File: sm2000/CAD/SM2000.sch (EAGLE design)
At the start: 405 parts, among them CN1 HDR100-3, CN2 ST-3509, CN3 HDR100-3, CN4 JS-MU3-002, CN5 DS-0518, CN6 ST-3509, CN7 ST-3509, J1 JMP-2PIN, J10 JMPR-2X2, J11 JMPR-2X2, J12 JMPR-2X2, J13 JMPR-2X2, J14 JMPR-2X2, J2 HDR100-7, J3 JMP-2PIN, J4 CONN-BOOM-XH-2A, J5 JMP-2PIN, J6 JMPR-2X2, J7 JMPR-2X2, J8 JMPR-2X2, J9 JMPR-2X2, P1 TPAD50, P10 TPAD50, P13 TPAD50, P2 TPAD50, P3 TPAD50, P4 TPAD50, P5 TPAD50, P6 TPAD50, P7 TPAD50, P8 TPAD50, P9 TPAD50, Q1 MMBT3904, Q10 MMBT3904, Q11 BFR92, Q12 BFQ19, Q13 RD01MUS2, Q14 MMBT3904, Q15 MMBT3904, Q16 MMBT3904, Q17 MMBT3906, Q2 STR2P3LLH6, Q3 MMBT3904, Q4 STR2P3LLH6, Q5 MMBT3904, Q6 MMBT3904, Q7 MMBT3904, Q8 MMBT3904, Q9 MMBT3904, SW1 TS-02B, SW2 SW-LC2259, SW3 TS-026, SW4 TS-026, SW5 SW-LC2259EENP, U1 STM32F405VGT6, U10 LM386M-1, U11 ADE-1, U12 PGA-103+, U13 LMV341, U14 SI5351A, U15 SI570, U16 SA612A, U2 STMPS2141, U3 EMIF02-USB03F2, U4 DNL, U5 L78MXX, U6 L78MXX, U7 LMV341, U8 AP7215Y-33, U9 TPS54329E, X1 BU-SMA-H

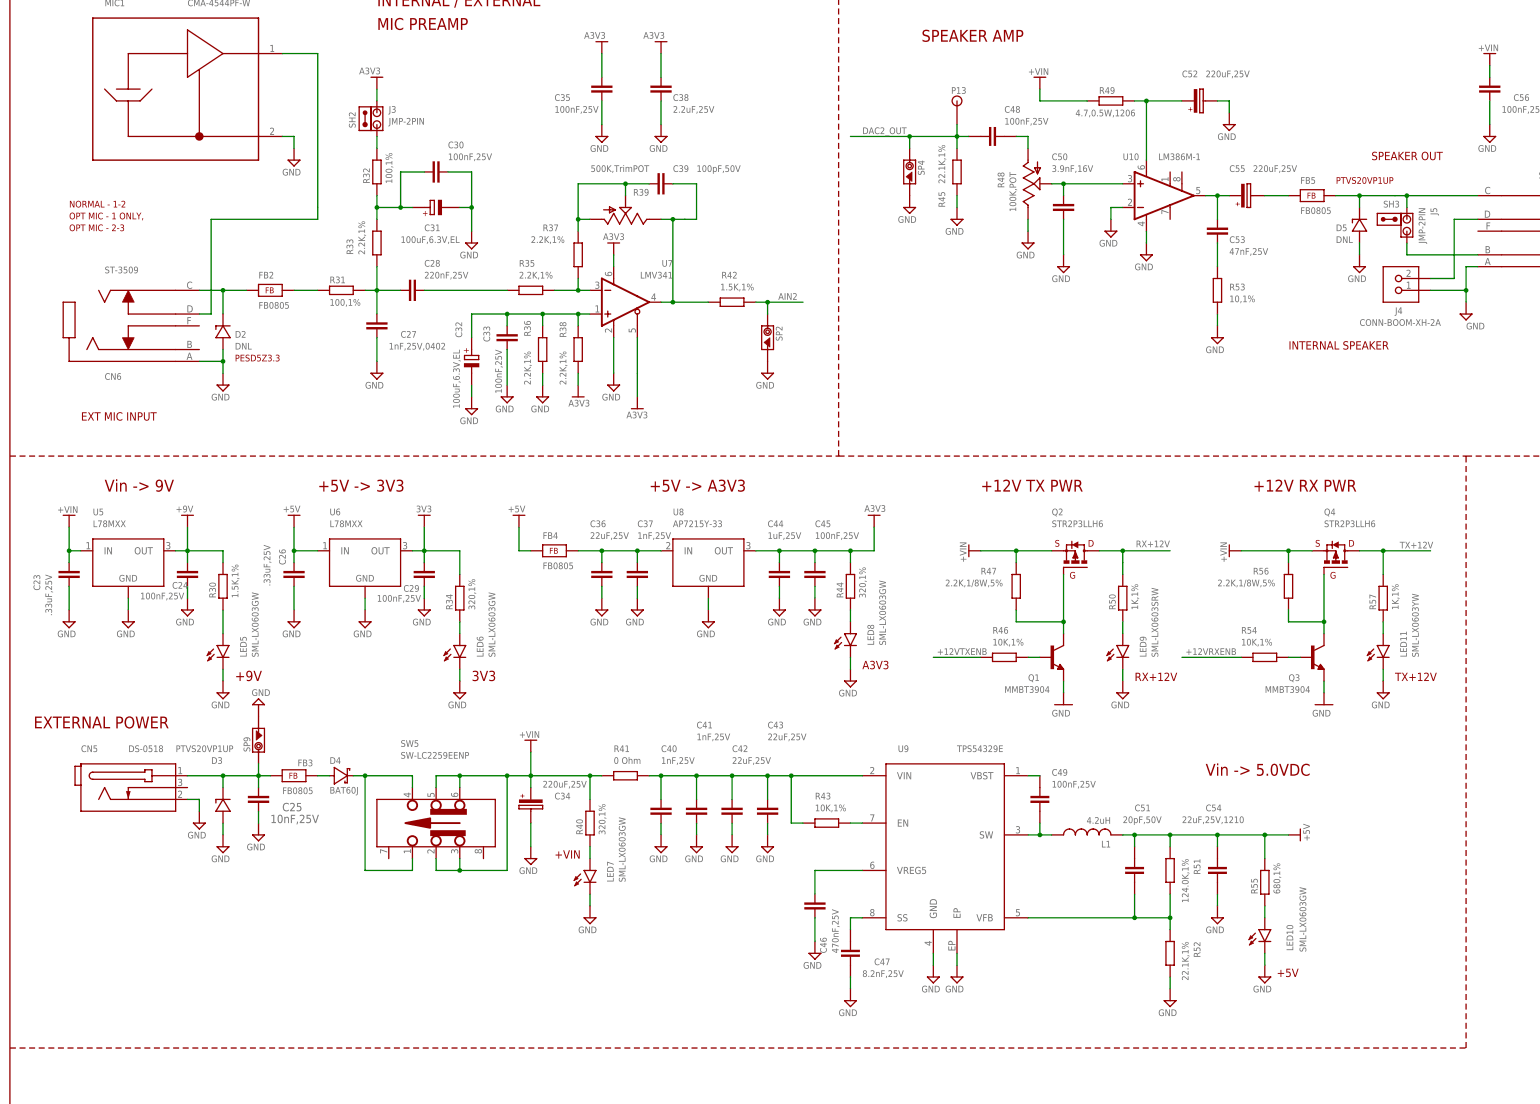
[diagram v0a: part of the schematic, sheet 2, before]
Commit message: Progress - Latest PCB block layouts. Plocks are identified and are moveable. Present loations are placeholders. Added netlist(NET-SM2000.txt),PDF schematic(SCH_SM2000.pdf) BOM PDF(BOM-SM2000.txt) and PDF of board file(BRD-SM2000.pdf). RGB
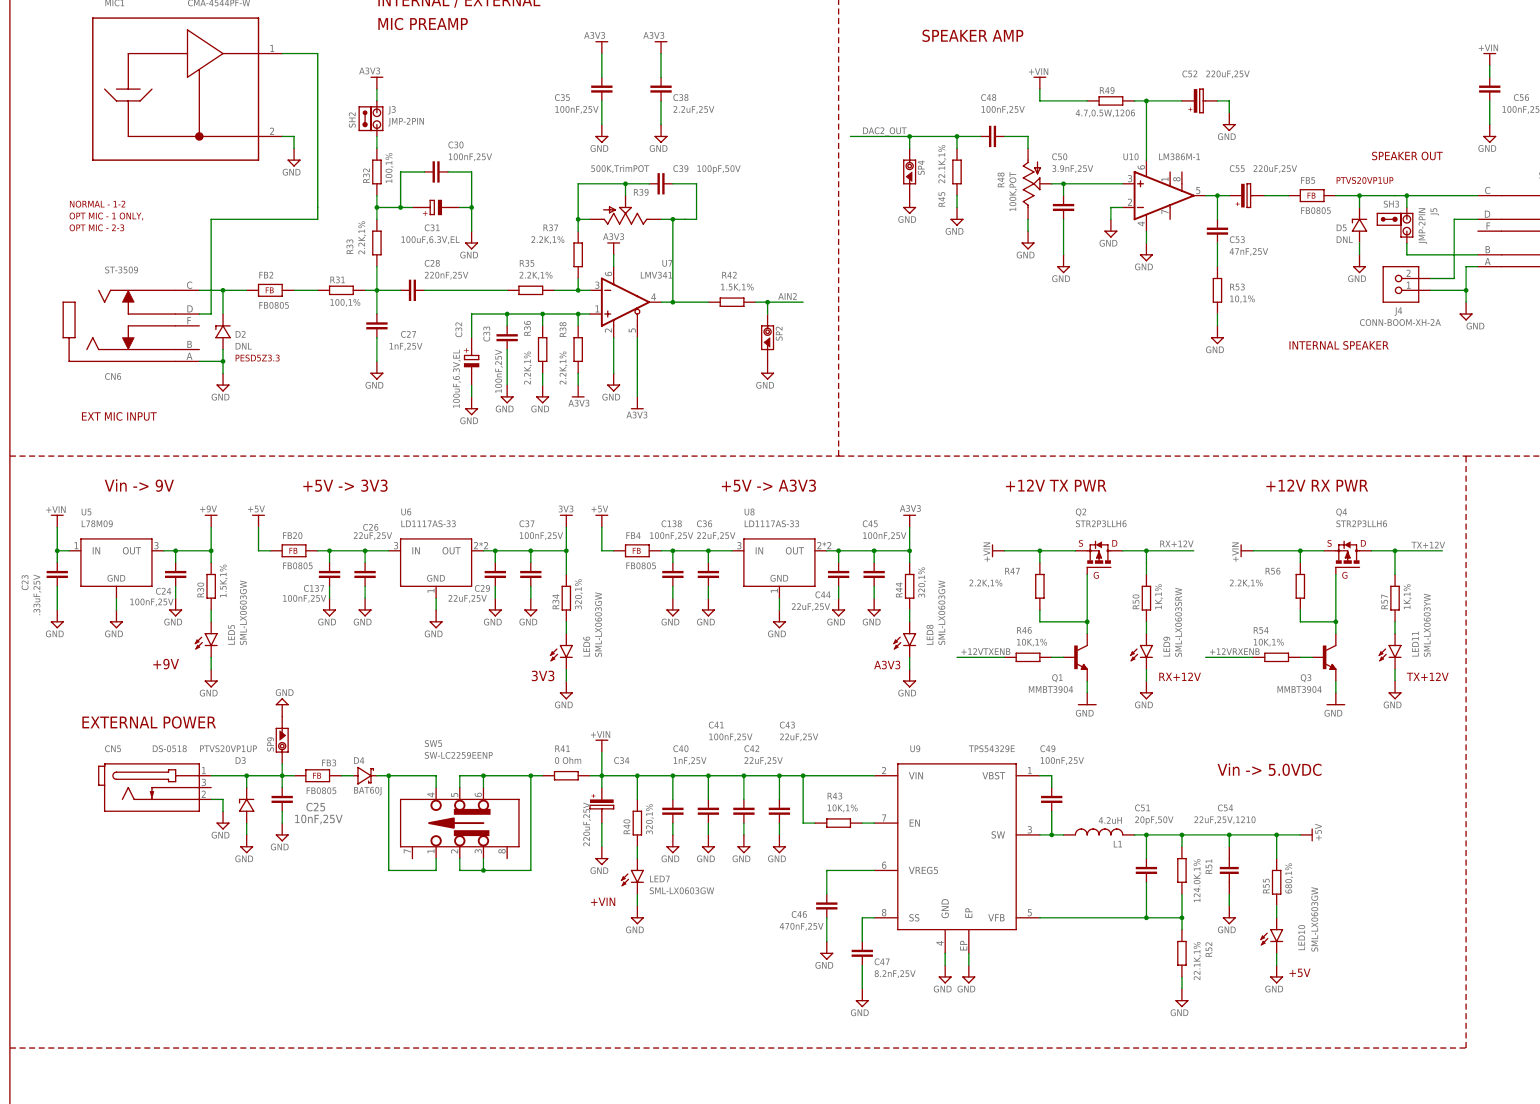
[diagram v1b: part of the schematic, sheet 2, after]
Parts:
- removed P13: TPAD50, _Coherix:TPAD50
- added C137, C138: 100nF,25V, _RoweTel:CAP-0805
- added FB20: FB0805, _RoweTel:FB0805
- C17, C18: value 2.2uF,16V -> 2.2uF,25V
- C22: value 4.7uF,16V,TANT -> 4.7uF,25V; device _RoweTel:CAP-TANT-1206 -> _RoweTel:CAP-0805
- C23, C24, C25, C40, C45, C46: device _RoweTel:CAP-0603 -> _RoweTel:CAP-0805
- C26: value .33uF,25V -> 22uF,25V; device _RoweTel:CAP-0603 -> _RoweTel:CAP-1210
- C27: value 1nF,25V,0402 -> 1nF,25V; device _RoweTel:CAP-0402 -> _RoweTel:CAP-0805
- C28, C30, C33, C35, C38, C39: device _RoweTel:CAP-0402 -> _RoweTel:CAP-0805
- C29: value 100nF,25V -> 22uF,25V; device _RoweTel:CAP-0603 -> _RoweTel:CAP-1210
- C37, C41: value 1nF,25V -> 100nF,25V; device _RoweTel:CAP-0603 -> _RoweTel:CAP-0805
- C42, C43: device _RoweTel:CAP-0603 -> _RoweTel:CAP-1210
- C44: value 1uF,25V -> 22uF,25V; device _RoweTel:CAP-0603 -> _RoweTel:CAP-1210
- C47: device AA-ipc-7351-capacitor:CAPACITOR_0603 -> _RoweTel:CAP-0805
- C48, C49, C51: device AA-ipc-7351-capacitor:CAPACITOR_0402 -> _RoweTel:CAP-0805
- C50: value 3.9nF,16V -> 3.9nF,25V
- C6, C7: value 1uF,16V -> 1uF,25V
- C77: value 1uF,25V,EL -> 1uF,25V; device _RoweTel:CAP-TANT-1206 -> _RoweTel:CAP-0805
- C95: value 22pF,25V -> 22pF,50V
- C99: value 1nF,25V -> 1nF,25V,DNL
- L18: value 9.2uH -> L-TDK-MLF-2012-9.2uH
- R1, R10, R11, R12, R13, R14, R16, R17, R18, R19, R2, R20, R21, R22, R23, R24, R25, R26, R27, R28, R29, R3, R30, R31, R32, R33, R34, R35, R36, R38, R4, R40, R41, R42, R43, R44, R45, R46, R5, R50, R51, R52, R53, R54, R55, R57, R6, R7, R8, R9: device _RoweTel:RES-0402 -> _RoweTel:RES-0805
- R37: device AA-ipc-7351-resistor:RESISTOR_0402 -> _RoweTel:RES-0805
- R47, R56: value 2.2K,1/8W,5% -> 2.2K,1%; device _RoweTel:RES-0402 -> _RoweTel:RES-0805
- R49: device AA-ipc-7351-resistor:RESISTOR_1206 -> _RoweTel:RES-1206
- U5: value L78MXX -> L78M09
- U6: value L78MXX -> LD1117AS-33; device _RoweTel:L78MXX -> _RoweTel:LD1117AS33
- U8: value AP7215Y-33 -> LD1117AS-33; device _RoweTel:AP7215Y -> _RoweTel:LD1117AS33
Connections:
- removed net N$399: C40.1, C41.1, C42.1, C43.1, R41.2, R43.1, U9.VIN
- new net N$110: C137.1, C26.1, FB20.2, U6.IN
- new net N$150: R41.1, SW5.2, SW5.3, SW5.5, SW5.6
- net +5V: now also FB20.1; no longer C26.1, U6.IN
- net +VIN: now also C40.1, C41.1, C42.1, C43.1, R41.2, R43.1, U9.VIN; no longer R41.1, SW5.2, SW5.3, SW5.5, SW5.6
- net 1ST_LO: now also U11.G1
- net 3V3: now also C37.1
- net DAC2_OUT: no longer P13.1
- net GND: now also C137.2, C138.2, L18.2; no longer L18.1
- net N$145: now also L18.1; no longer L18.2
- net N$54: now also C138.1; no longer C37.1
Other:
- note added: "Load/Adjust R92/C99 if PA stability is a problem"
- note removed: "1st LO"
- note removed: "DNL"
- note removed: "Load/Adjust R98/C95 if PA stability is a problem"
- moved on the sheet: C23, C24, C25, C26, C29, C34, C36, C37, C40, C41, C42, C43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

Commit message: Progress Update. Working on Driver_PA block. RGB
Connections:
- net GND: now also Q13.S2
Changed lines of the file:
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@@
 <wire x1="297.18" y1="63.5" x2="297.18" y2="58.42" width="0.1524" layer="91"/>
 <pinref part="Q13" gate="G$1" pin="S"/>
-<wire x1="309.88" y1="78.74" x2="309.88" y2="58.42" width="0.1524" layer="91"/>
+<wire x1="309.88" y1="78.74" x2="309.88" y2="76.2" width="0.1524" layer="91"/>
 <pinref part="C105" gate="G$1" pin="2"/>
+<wire x1="309.88" y1="76.2" x2="309.88" y2="58.42" width="0.1524" layer="91"/>
 <wire x1="322.58" y1="91.44" x2="322.58" y2="86.36" width="0.1524" layer="91"/>
 <wire x1="322.58" y1="86.36" x2="322.58" y2="58.42" width="0.1524" layer="91"/>
@@
 <junction x="297.18" y="58.42"/>
 <junction x="309.88" y="58.42"/>
+<pinref part="Q13" gate="G$1" pin="S2"/>
+<wire x1="314.96" y1="78.74" x2="314.96" y2="76.2" width="0.1524" layer="91"/>
+<wire x1="314.96" y1="76.2" x2="309.88" y2="76.2" width="0.1524" layer="91"/>
+<junction x="309.88" y="76.2"/>
 </segment>
 <segment>

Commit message: Progress update and backup. Power supplies laid out. CPU, Mic preamp & Speaker amp next. Looks like adequate room for RF blocks. RGB
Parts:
- removed C83, C88: 2.2pF,50V, _RoweTel:CAP-0805
- removed L7: 260nH, rcl:L-US0204/5
- D4: value BAT60J -> B330B; device _RoweTel:BAT60J -> _RoweTel:B330B
- LED7: value SML-LX0603GW -> LTST-S220KGKT; device _RoweTel:SML-LX0603SRW -> _RoweTel:LTST-S220K
- XTAL3, XTAL4: device _RoweTel:ECS-10.7-15B -> _RoweTel:ECS-10.7-15BECS-10.7-12A
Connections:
- removed net N$139: C83.1, C88.2, L7.1
- removed net N$30: C88.1
- removed net N$36: C83.2
- net GND: now also XTAL3.2, XTAL4.2; no longer L7.2
- net N$143: now also XTAL3.3; no longer XTAL3.1
- net N$144: now also XTAL3.1, XTAL4.1; no longer XTAL3.2, XTAL4.2
- net N$145: now also XTAL4.3; no longer XTAL4.1
- net N$81: now also D4.K; no longer D4.C
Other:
- note added: "2.2pF.50V"
- note added: "260nH"
- note added: "GND"
- note added: "L5 and L8 at right angles with shield"
- note added: "Tune L5 and L8 to 146MHz"
- note removed: "L1 and L2 at right angles with shield"
- note removed: "Tune L1 and L2 to 146MHz"
- moved on the sheet: C112, L18

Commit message: Latest schematic, PCB and associated files. Represents work through 03/11/2016  RGB
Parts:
- removed C116: 2-12pF, c-trimm:C-TRIMM3008
- removed P1, P10, P2, P3, P4, P5: TPAD50, _Coherix:TPAD50
- added C83: 2-12pF, _RoweTel:TRIMCAP_VAR_2222_V
- C104, C108, C125, C84, C90, C94: value 0.1uF.25V -> 100nF,25V
- C111, C113, C114, C117, C118, C119, C120, C121, C127, C133, C134: value 0.1uF,25V -> 100nF,25V
- C16: value 1uF,16V -> 1uF,25V
- C54: value 22uF,25V,1210 -> 22uF,25V; device AA-ipc-7351-capacitor:CAPACITOR_1210 -> _RoweTel:CAP-1210
- C64: value 12pF.50V -> 12pF,50V
- L20: value 15uH -> 15uH,TDK,MLF
- R34, R40, R44: value 320,1% -> 330,1%
- XTAL1: value XTAL-FY0800035 -> 8.000MHz; device _RoweTel:XTAL-FY0800035 -> _RoweTel:CTS-405
- XTAL2: value 25MHz,TXC,SMD -> 25.000MHz; device _RoweTel:XTAL-FY0800035 -> _RoweTel:CTS-405
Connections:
- net N$12 renamed VDDA
- net N$2 renamed VBAT
- net N$5 renamed VREF+
- new net N$2: U14.XA
- net +12VRXENB: now also R46.1; no longer R54.1
- net +12VTXENB: now also R54.1; no longer R46.1
- net +5V: no longer P5.1
- net +VIN: no longer P10.1
- net 3V3: no longer P1.1
- net GND: now also C83.S; no longer C116.A, P2.1, P3.1, P4.1, XTAL1.2
- net N$145: now also C83.R; no longer C116.E
- net N$65: now also XTAL2.1; no longer U14.XA, XTAL2.3
- net N$80: now also XTAL2.3; no longer XTAL2.1
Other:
- note removed: "PTT FUNCTION"
- moved on the sheet: R13, R14

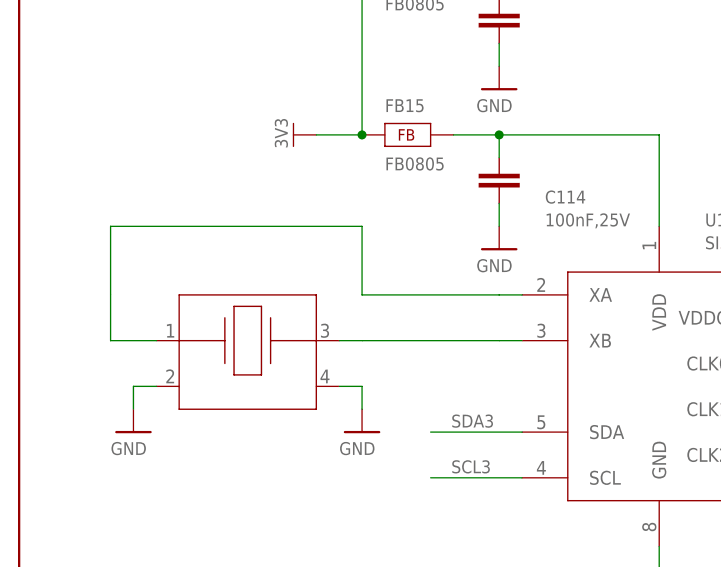
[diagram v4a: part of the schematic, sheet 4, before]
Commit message: Updating to current status. Moved parts onto brd and made BOM current. RGB
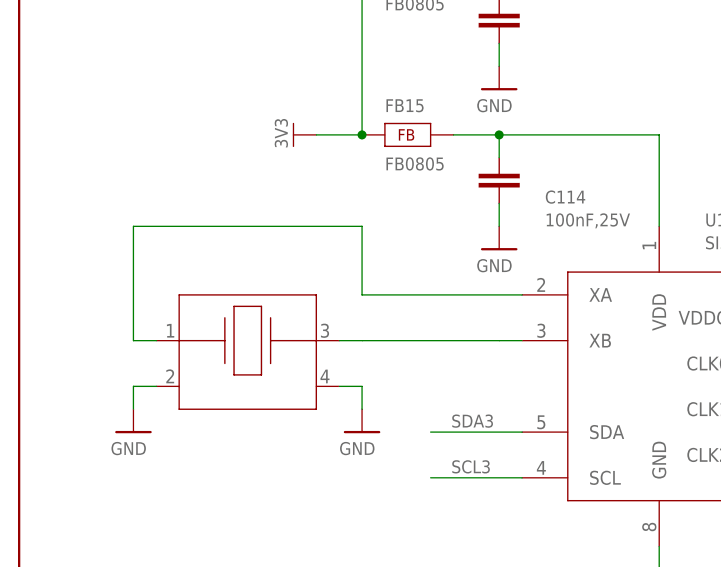
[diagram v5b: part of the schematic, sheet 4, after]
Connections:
- removed net N$65: XTAL2.1
- net GND: now also XTAL1.2
- net N$2: now also XTAL2.1
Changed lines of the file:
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@@
 <net name="3V3" class="0">
 <segment>
-<wire x1="101.6" y1="30.48" x2="104.14" y2="30.48" width="0.1524" layer="91"/>
-<wire x1="104.14" y1="30.48" x2="99.06" y2="30.48" width="0.1524" layer="91"/>
 <wire x1="99.06" y1="30.48" x2="86.36" y2="30.48" width="0.1524" layer="91"/>
 <wire x1="86.36" y1="30.48" x2="73.66" y2="30.48" width="0.1524" layer="91"/>
@@
 <junction x="60.96" y="30.48"/>
 <junction x="73.66" y="30.48"/>
-<pinref part="R14" gate="G$1" pin="1"/>
 <wire x1="10.16" y1="30.48" x2="10.16" y2="60.96" width="0.1524" layer="91"/>
 <junction x="10.16" y="30.48"/>
@@
 <wire x1="99.06" y1="22.86" x2="99.06" y2="30.48" width="0.1524" layer="91"/>
 <junction x="86.36" y="30.48"/>
-<junction x="99.06" y="30.48"/>
 <pinref part="V11" gate="G$1" pin="3V3"/>
+<pinref part="R14" gate="G$1" pin="1"/>
+<wire x1="99.06" y1="30.48" x2="101.6" y2="30.48" width="0.1524" layer="91"/>
+<junction x="99.06" y="30.48"/>
 </segment>
 <segment>
@@
 </segment>
 <segment>
-<wire x1="226.06" y1="190.5" x2="223.52" y2="190.5" width="0.1524" layer="91"/>
-<wire x1="223.52" y1="190.5" x2="223.52" y2="180.34" width="0.1524" layer="91"/>
-<pinref part="V51" gate="GND" pin="GND"/>
-</segment>
-<segment>
 <wire x1="246.38" y1="190.5" x2="248.92" y2="190.5" width="0.1524" layer="91"/>
 <wire x1="248.92" y1="190.5" x2="248.92" y2="180.34" width="0.1524" layer="91"/>
@@
 <pinref part="V88" gate="GND" pin="GND"/>
 </segment>
+<segment>
+<pinref part="XTAL1" gate="G$1" pin="2"/>
+<pinref part="V51" gate="GND" pin="GND"/>
+<wire x1="226.06" y1="190.5" x2="223.52" y2="190.5" width="0.1524" layer="91"/>
+<wire x1="223.52" y1="190.5" x2="223.52" y2="180.34" width="0.1524" layer="91"/>
+</segment>
 </net>
 <net name="NRST" class="0">
@@
 </segment>
 </net>
-<net name="N$65" class="0">
-<segment>
-<wire x1="38.1" y1="114.3" x2="38.1" y2="121.92" width="0.1524" layer="91"/>
-<wire x1="38.1" y1="121.92" x2="10.16" y2="121.92" width="0.1524" layer="91"/>
-<wire x1="10.16" y1="121.92" x2="10.16" y2="114.3" width="0.1524" layer="91"/>
-<wire x1="10.16" y1="114.3" x2="10.16" y2="109.22" width="0.1524" layer="91"/>
-<wire x1="10.16" y1="109.22" x2="15.24" y2="109.22" width="0.1524" layer="91"/>
-<pinref part="XTAL2" gate="G$1" pin="1"/>
-</segment>
-</net>
 <net name="N$80" class="0">
 <segment>
@@
 <segment>
 <pinref part="U14" gate="G$1" pin="XA"/>
-<wire x1="55.88" y1="114.3" x2="53.34" y2="114.3" width="0.1524" layer="91"/>
-<wire x1="53.34" y1="114.3" x2="38.1" y2="114.3" width="0.1524" layer="91"/>
+<wire x1="55.88" y1="114.3" x2="38.1" y2="114.3" width="0.1524" layer="91"/>
+<wire x1="38.1" y1="114.3" x2="38.1" y2="121.92" width="0.1524" layer="91"/>
+<wire x1="38.1" y1="121.92" x2="12.7" y2="121.92" width="0.1524" layer="91"/>
+<wire x1="12.7" y1="121.92" x2="12.7" y2="109.22" width="0.1524" layer="91"/>
+<pinref part="XTAL2" gate="G$1" pin="1"/>
+<wire x1="12.7" y1="109.22" x2="15.24" y2="109.22" width="0.1524" layer="91"/>
 </segment>
 </net>
@@
 </sheet>
 </sheets>
+<errors>
+</errors>
 </schematic>
 </drawing>
